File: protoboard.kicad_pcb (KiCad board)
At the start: 2 copper layers, 50 x 50 mm, 1755 parts, among them P1 PAD, P10 PAD, P11 PAD, P12 PAD, P13 PAD, P14 PAD, P15 PAD, P16 PAD, P17 PAD, P18 PAD, P19 PAD, P2 PAD, P20 PAD, P21 PAD, P22 PAD, P23 PAD, P24 PAD, P25 PAD, P26 PAD, P27 PAD, P28 PAD, P29 PAD, P3 PAD, P30 PAD, P31 PAD, P32 PAD, P33 PAD, P34 PAD, P35 PAD, P36 PAD, P37 PAD, P38 PAD, P39 PAD, P4 PAD, P40 PAD, P41 PAD, P42 PAD, P43 PAD, P44 PAD, P45 PAD, P5 PAD, P6 PAD, P7 PAD, P8 PAD, P9 PAD, U1 PROTO_SOIC6, U10 PROTO_SOT23, U100 PAD, U1000 PAD, U1001 PAD, U1002 PAD, U1003 PAD, U1004 PAD, U1005 PAD, U1006 PAD, U1007 PAD, U1008 PAD, U1009 PAD, U101 PAD, U1010 PAD, U1011 PAD, U1012 PAD, U1013 PAD, U1014 PAD, U1015 PAD, U1016 PAD, U1017 PAD, U1018 PAD, U1019 PAD, U102 PAD, U1020 PAD, U1021 PAD, U1022 PAD, U1023 PAD, U1024 PAD, U1025 PAD, U1026 PAD, U1027 PAD, U1028 PAD, U1029 PAD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

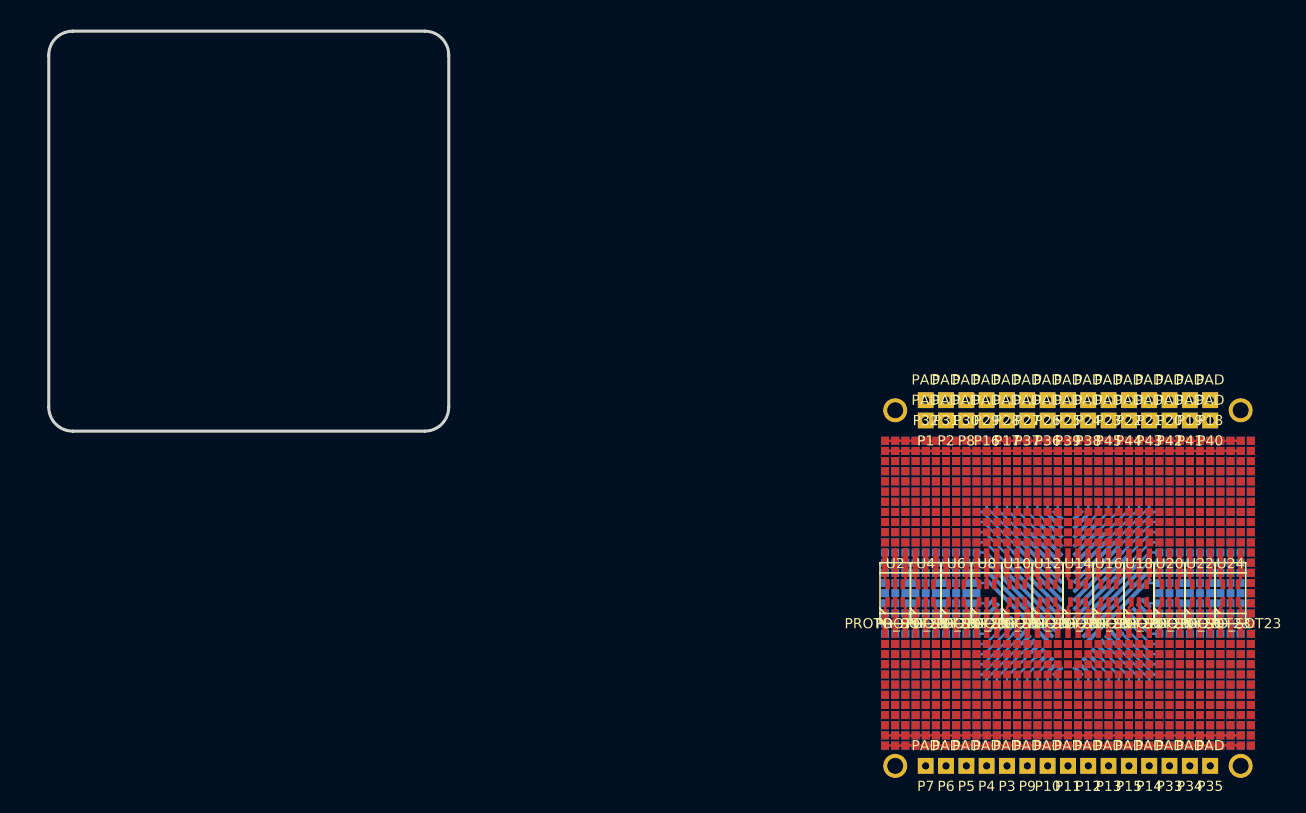
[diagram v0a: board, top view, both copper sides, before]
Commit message: Position board within curved edge cuts
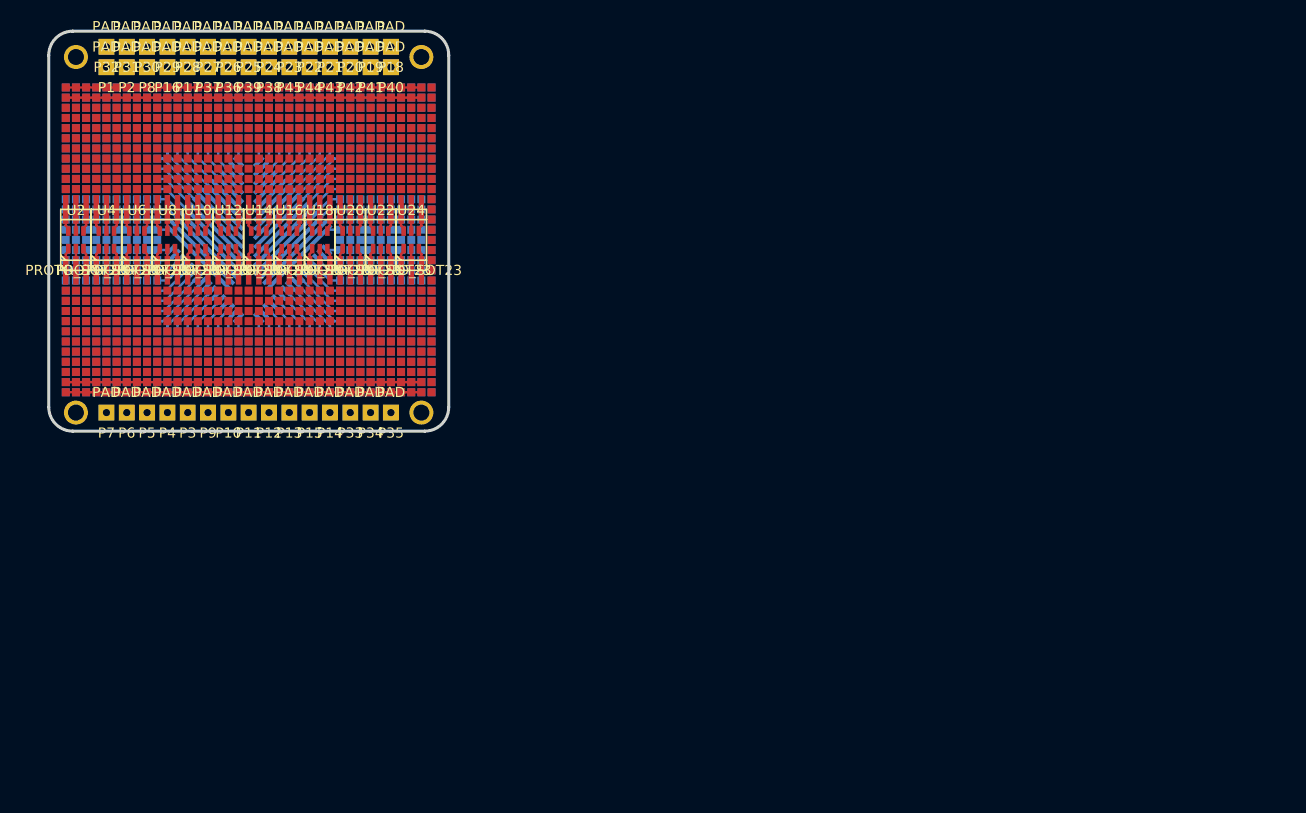
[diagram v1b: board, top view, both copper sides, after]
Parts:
- moved H2 111.5 mm to (71.6, 72.7)
- moved H4 111.5 mm to (71.6, 28.2)
- moved P10 111.5 mm to (47.5, 72.7)
- moved P15 111.5 mm to (57.6, 72.7)
- moved P16 111.5 mm to (39.8, 29.5)
- moved P18 111.5 mm to (67.8, 27.0)
- moved P22 111.5 mm to (57.6, 27.0)
- moved P26 111.5 mm to (47.5, 27.0)
- moved P29 111.5 mm to (39.8, 27.0)
- moved P35 111.5 mm to (67.8, 72.7)
- moved P36 111.5 mm to (47.5, 29.5)
- moved P4 111.5 mm to (39.8, 72.7)
- moved P40 111.5 mm to (67.8, 29.5)
- moved P44 111.5 mm to (57.6, 29.5)
- moved PT2 111.5 mm to (47.5, 62.5)
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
